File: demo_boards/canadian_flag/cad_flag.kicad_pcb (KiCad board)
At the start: 2 copper layers, 70 x 35 mm, 5 parts, among them J1 Conn_01x12, J2 USB_B, J3 Conn_01x12, U1 SAMD21_MOD

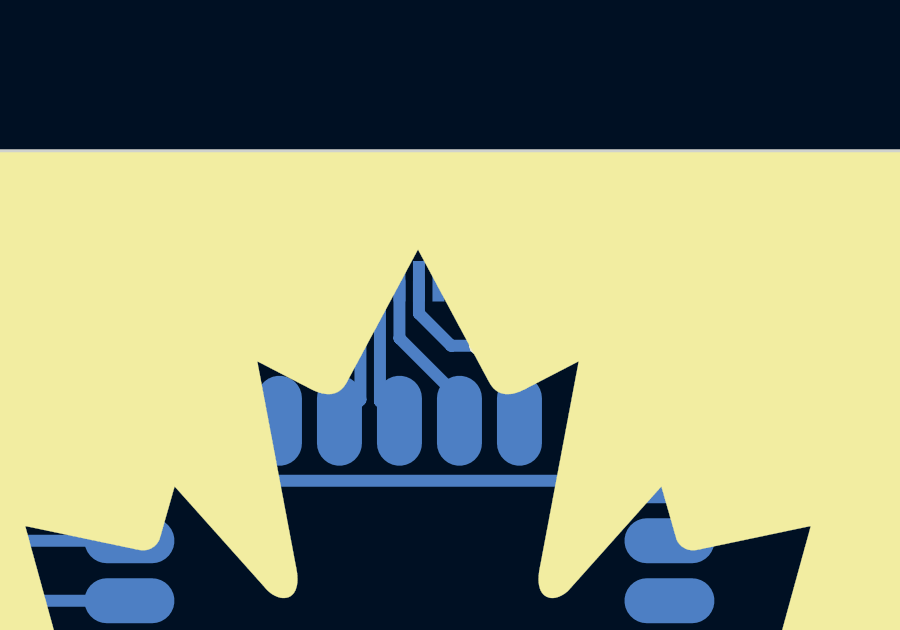
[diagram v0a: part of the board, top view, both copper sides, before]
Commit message: fixed usb connector
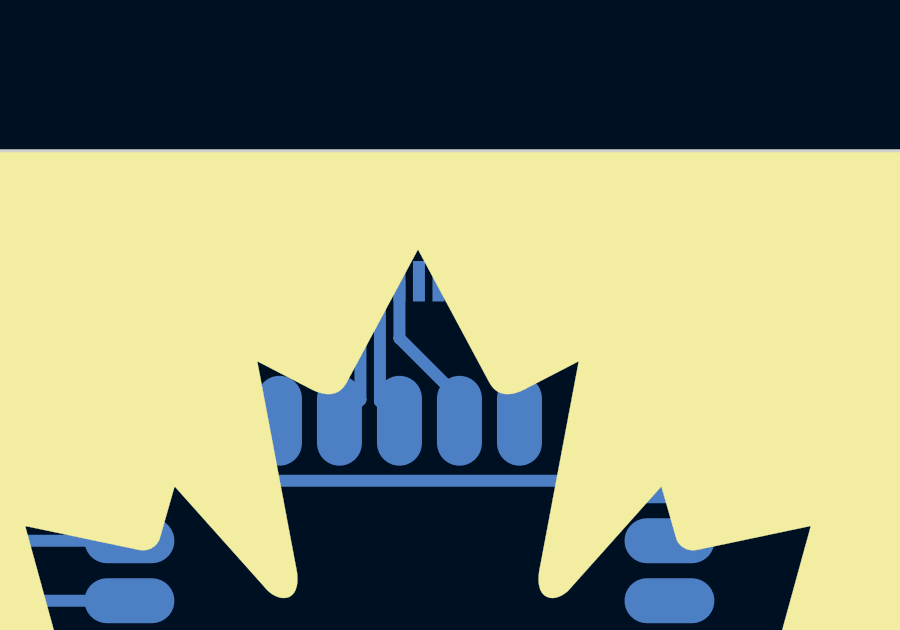
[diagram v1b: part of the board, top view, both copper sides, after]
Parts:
- J2: value USB_B -> USB_OTG
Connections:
- J2 pad 4: GND -> Net-(J2-Pad4)
- J2 pad 5: Net-(J2-Pad5) -> GND
- J2 pad 6: (no net) -> Net-(J2-Pad6)
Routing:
- net GND: track 9.44 -> 5.95 mm, vias 2 -> 1
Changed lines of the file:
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@@
-(kicad_pcb (version 4) (host pcbnew 4.0.4-stable)
+(kicad_pcb (version 4) (host pcbnew 4.0.7)
   (general
-    (links 29)
-    (no_connects 0)
-    (area 61.42 50.05 184.141484 171.150001)
+    (links 36)
+    (no_connects 5)
+    (area 100.569999 65.299999 170.670001 100.400001)
     (thickness 1.6)
     (drawings 6)
-    (tracks 75)
+    (tracks 71)
     (zones 0)
     (modules 5)
-    (nets 32)
+    (nets 33)
   )
   (page A3)
@@
   (net 27 +BATT)
   (net 28 "Net-(J2-Pad2)")
-  (net 29 "Net-(J2-Pad5)")
-  (net 30 "Net-(J2-Pad3)")
-  (net 31 "Net-(J2-Pad1)")
+  (net 29 "Net-(J2-Pad3)")
+  (net 30 "Net-(J2-Pad1)")
+  (net 31 "Net-(J2-Pad6)")
+  (net 32 "Net-(J2-Pad4)")
   (net_class Default "This is the default net class."
     (clearance 0.15)
@@
     (add_net "Net-(J2-Pad2)")
     (add_net "Net-(J2-Pad3)")
-    (add_net "Net-(J2-Pad5)")
+    (add_net "Net-(J2-Pad4)")
+    (add_net "Net-(J2-Pad6)")
     (add_net RESET)
     (add_net RX/D0)
@@
       (effects (font (size 1 1) (thickness 0.15)) (justify mirror))
     )
-    (fp_text value USB_B (at 0.3 -3.45) (layer B.Fab)
+    (fp_text value USB_OTG (at 0.3 -3.45) (layer B.Fab)
       (effects (font (size 1 1) (thickness 0.15)) (justify mirror))
     )
@@
     (fp_line (start -1.5 3.01) (end -1.5 2.8) (layer B.Fab) (width 0.1))
     (fp_line (start -1.1 3.01) (end -1.1 2.8) (layer B.Fab) (width 0.1))
-    (pad 6 smd rect (at 1 -0.35) (size 1.5 1.9) (layers B.Cu B.Paste B.Mask))
-    (pad 6 thru_hole circle (at -2.5 2.35) (size 1.45 1.45) (drill 0.85) (layers *.Cu *.Mask))
+    (pad 6 smd rect (at 1 -0.35) (size 1.5 1.9) (layers B.Cu B.Paste B.Mask)
+      (net 31 "Net-(J2-Pad6)"))
+    (pad 6 thru_hole circle (at -2.5 2.35) (size 1.45 1.45) (drill 0.85) (layers *.Cu *.Mask)
+      (net 31 "Net-(J2-Pad6)"))
     (pad 2 smd rect (at -0.65 2.35) (size 0.4 1.35) (layers B.Cu B.Paste B.Mask)
       (net 28 "Net-(J2-Pad2)"))
     (pad 1 smd rect (at -1.3 2.35) (size 0.4 1.35) (layers B.Cu B.Paste B.Mask)
-      (net 31 "Net-(J2-Pad1)"))
+      (net 30 "Net-(J2-Pad1)"))
     (pad 5 smd rect (at 1.3 2.35) (size 0.4 1.35) (layers B.Cu B.Paste B.Mask)
-      (net 29 "Net-(J2-Pad5)"))
+      (net 1 GND))
     (pad 4 smd rect (at 0.65 2.35) (size 0.4 1.35) (layers B.Cu B.Paste B.Mask)
-      (net 1 GND))
+      (net 32 "Net-(J2-Pad4)"))
     (pad 3 smd rect (at 0 2.35) (size 0.4 1.35) (layers B.Cu B.Paste B.Mask)
-      (net 30 "Net-(J2-Pad3)"))
-    (pad 6 thru_hole circle (at 2.5 2.35) (size 1.45 1.45) (drill 0.85) (layers *.Cu *.Mask))
-    (pad 6 smd rect (at -1 -0.35) (size 1.5 1.9) (layers B.Cu B.Paste B.Mask))
-    (pad 6 thru_hole oval (at -3.5 -0.35 180) (size 1.2 1.9) (drill oval 0.6 1.3) (layers *.Cu *.Mask))
-    (pad 6 thru_hole oval (at 3.5 -0.35) (size 1.2 1.9) (drill oval 0.6 1.3) (layers *.Cu *.Mask))
-    (pad 6 smd rect (at 2.9 -0.35) (size 1.2 1.9) (layers B.Cu B.Mask))
-    (pad 6 smd rect (at -2.9 -0.35) (size 1.2 1.9) (layers B.Cu B.Mask))
+      (net 29 "Net-(J2-Pad3)"))
+    (pad 6 thru_hole circle (at 2.5 2.35) (size 1.45 1.45) (drill 0.85) (layers *.Cu *.Mask)
+      (net 31 "Net-(J2-Pad6)"))
+    (pad 6 smd rect (at -1 -0.35) (size 1.5 1.9) (layers B.Cu B.Paste B.Mask)
+      (net 31 "Net-(J2-Pad6)"))
+    (pad 6 thru_hole oval (at -3.5 -0.35 180) (size 1.2 1.9) (drill oval 0.6 1.3) (layers *.Cu *.Mask)
+      (net 31 "Net-(J2-Pad6)"))
+    (pad 6 thru_hole oval (at 3.5 -0.35) (size 1.2 1.9) (drill oval 0.6 1.3) (layers *.Cu *.Mask)
+      (net 31 "Net-(J2-Pad6)"))
+    (pad 6 smd rect (at 2.9 -0.35) (size 1.2 1.9) (layers B.Cu B.Mask)
+      (net 31 "Net-(J2-Pad6)"))
+    (pad 6 smd rect (at -2.9 -0.35) (size 1.2 1.9) (layers B.Cu B.Mask)
+      (net 31 "Net-(J2-Pad6)"))
     (model ${KISYS3DMOD}/Connectors_USB.3dshapes/USB_Micro-B_Molex-105017-0001.wrl
       (at (xyz 0 0 0))
@@
       (net 26 D4))
     (pad 30 smd oval (at -2 11 270) (size 3 1.5) (layers B.Cu B.Mask)
-      (net 30 "Net-(J2-Pad3)"))
+      (net 29 "Net-(J2-Pad3)"))
     (pad 28 smd oval (at 2 11 270) (size 3 1.5) (layers B.Cu B.Mask)
-      (net 31 "Net-(J2-Pad1)"))
+      (net 30 "Net-(J2-Pad1)"))
     (pad 31 smd oval (at -4 11 270) (size 3 1.5) (layers B.Cu B.Mask)
       (net 1 GND))
@@
   (segment (start 137.62 71.85) (end 139 73.23) (width 0.4) (layer B.Cu) (net 1))
   (segment (start 139 73.23) (end 139 74.35) (width 0.4) (layer B.Cu) (net 1))
-  (segment (start 135.65 69.7) (end 135.65 70.775) (width 0.4) (layer B.Cu) (net 1))
-  (segment (start 135.65 70.775) (end 136.725 71.85) (width 0.4) (layer B.Cu) (net 1))
-  (via (at 137.62 71.85) (size 0.6) (drill 0.4) (layers F.Cu B.Cu) (net 1))
-  (segment (start 136.725 71.85) (end 137.62 71.85) (width 0.4) (layer B.Cu) (net 1))
   (segment (start 144 86.35) (end 155.88 86.35) (width 0.4) (layer B.Cu) (net 2))
   (segment (start 155.88 86.35) (end 168.62 73.61) (width 0.4) (layer B.Cu) (net 2))
@@
   (segment (start 134.35 69.7) (end 134.35 73.7) (width 0.4) (layer B.Cu) (net 28))
   (segment (start 134.35 73.7) (end 135 74.35) (width 0.4) (layer B.Cu) (net 28))
-  (segment (start 135 69.7) (end 135 71.6) (width 0.4) (layer B.Cu) (net 30))
-  (segment (start 135 71.6) (end 137 73.6) (width 0.4) (layer B.Cu) (net 30))
-  (segment (start 137 73.6) (end 137 74.35) (width 0.4) (layer B.Cu) (net 30))
-  (segment (start 133.7 69.7) (end 133.7 73.65) (width 0.4) (layer B.Cu) (net 31))
-  (segment (start 133.7 73.65) (end 133 74.35) (width 0.4) (layer B.Cu) (net 31))
+  (segment (start 135 69.7) (end 135 71.6) (width 0.4) (layer B.Cu) (net 29))
+  (segment (start 135 71.6) (end 137 73.6) (width 0.4) (layer B.Cu) (net 29))
+  (segment (start 137 73.6) (end 137 74.35) (width 0.4) (layer B.Cu) (net 29))
+  (segment (start 133.7 69.7) (end 133.7 73.65) (width 0.4) (layer B.Cu) (net 30))
+  (segment (start 133.7 73.65) (end 133 74.35) (width 0.4) (layer B.Cu) (net 30))
   (zone (net 1) (net_name GND) (layer F.Cu) (hatch edge 0.508)
     (connect_pads (clearance 0.15))
